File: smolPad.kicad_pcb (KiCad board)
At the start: 2 copper layers, 83.5 x 76.5 mm, 25 parts, among them U1 ProMicro

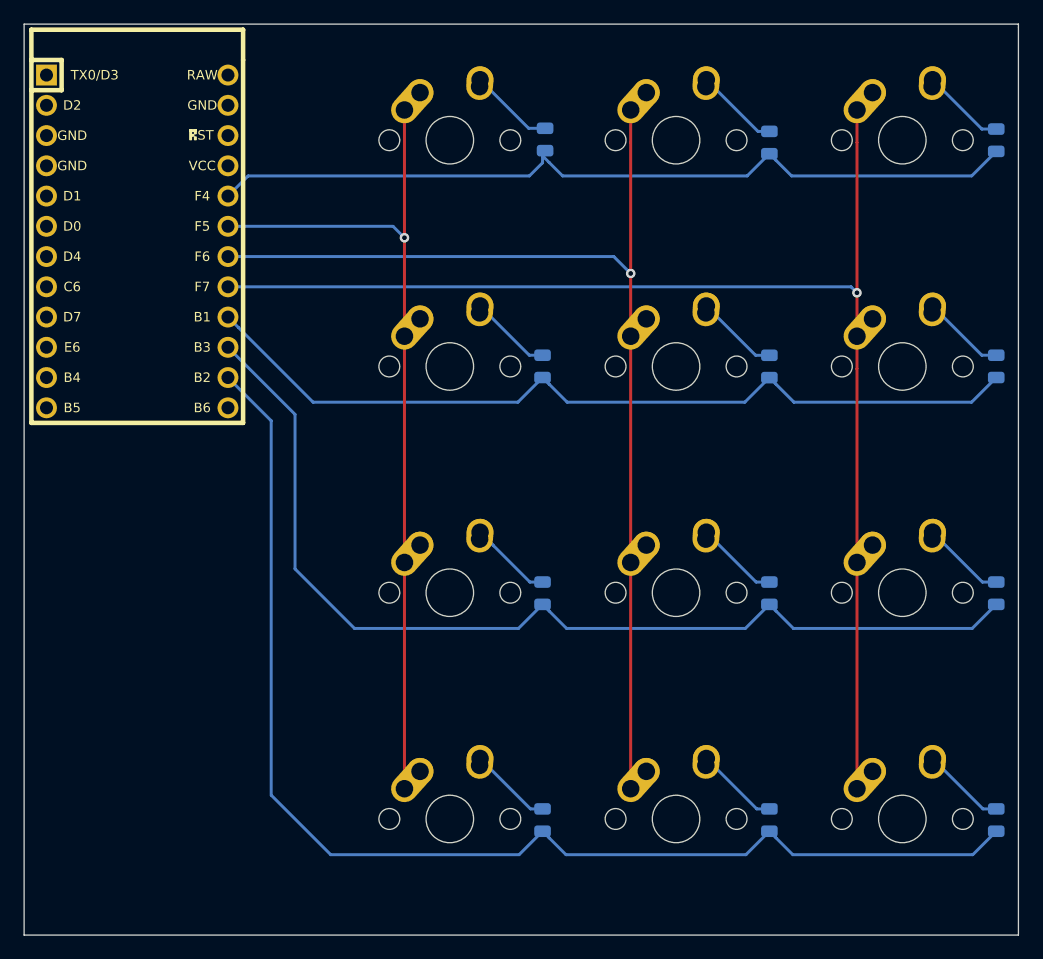
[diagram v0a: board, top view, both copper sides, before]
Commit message: Updated design to use both THT and SMD Diodes. Silkscreen added as well.
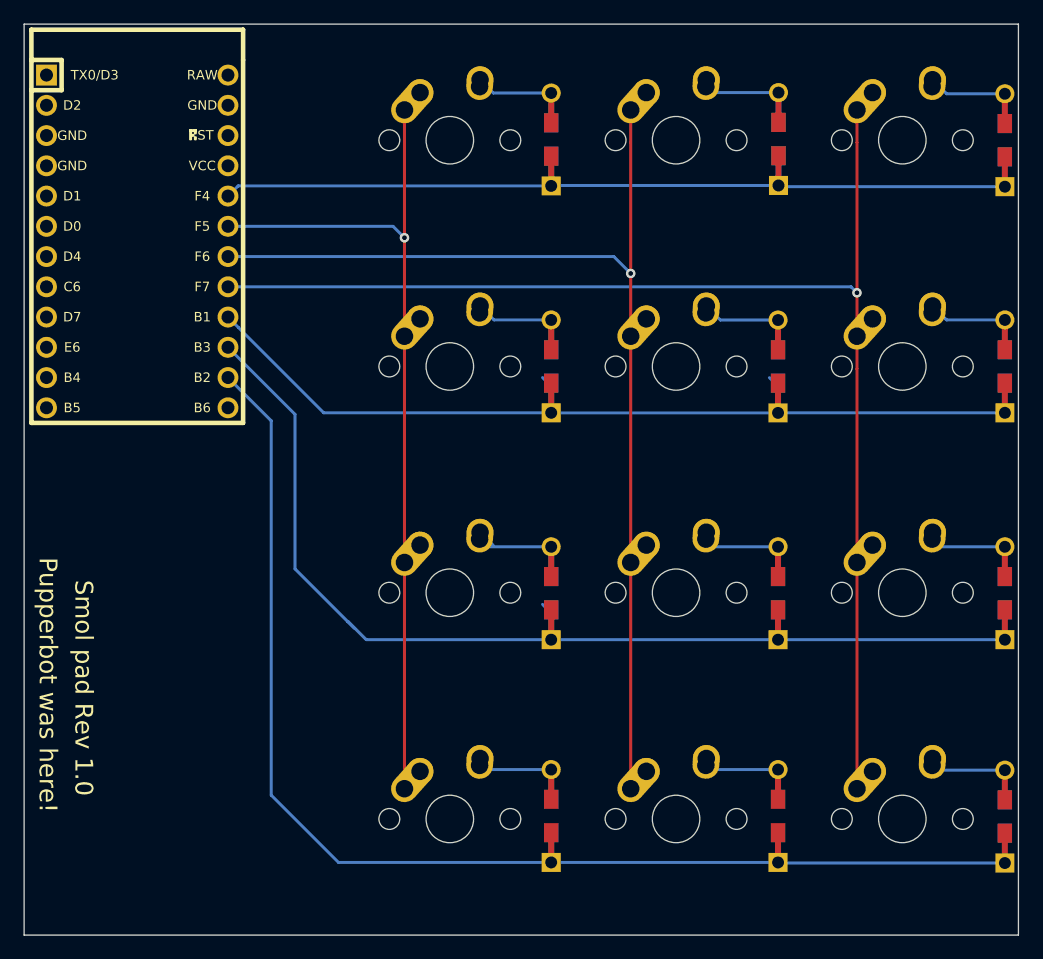
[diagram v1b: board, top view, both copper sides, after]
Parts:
- D1, D10, D11, D12, D2, D3, D4, D5, D6, D7, D8, D9: footprint Diode_SMD:D_0805_2012Metric -> Keebio-Parts:Diode-dual
- moved D2 0.82 mm to (182.6, 59.9), turned to 270 degrees
- moved D10 0.80 mm to (163.5, 116.8), turned to 270 degrees
- moved D11 0.80 mm to (182.6, 116.8), turned to 270 degrees
- moved D12 0.78 mm to (201.6, 116.8), turned to 270 degrees
- moved D3 0.73 mm to (201.6, 60.0), turned to 270 degrees
- moved D6 0.73 mm to (201.6, 79.0), turned to 270 degrees
- moved D9 0.73 mm to (201.6, 98.0), turned to 270 degrees
- moved D4 0.73 mm to (163.5, 79.0), turned to 270 degrees
- moved D5 0.73 mm to (182.6, 79.0), turned to 270 degrees
- moved D7 0.73 mm to (163.5, 98.0), turned to 270 degrees
- moved D8 0.73 mm to (182.6, 98.0), turned to 270 degrees
- moved D1 0.51 mm to (163.5, 59.9), turned to 270 degrees
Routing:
- net ROW0: track 69.4 -> 65.7 mm
- net ROW3: track 103.6 -> 100.5 mm
- net ROW1: track 71.8 -> 70.2 mm
- net ROW2: track 86.1 -> 84.6 mm
- net Net-(D3-Pad2): track 6.86 -> 6.36 mm
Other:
- board text added: "Pupperbot was here!"
- board text added: "Smol pad Rev 1.0"
